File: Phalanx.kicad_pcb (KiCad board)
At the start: 2 copper layers, 19 x 95.2 mm, 7 parts, among them J1 Conn_01x05, J2 Conn_01x05, J3 Conn_01x05, SW1 SW_Push, SW2 SW_Push, SW3 SW_Push, SW4 SW_Push

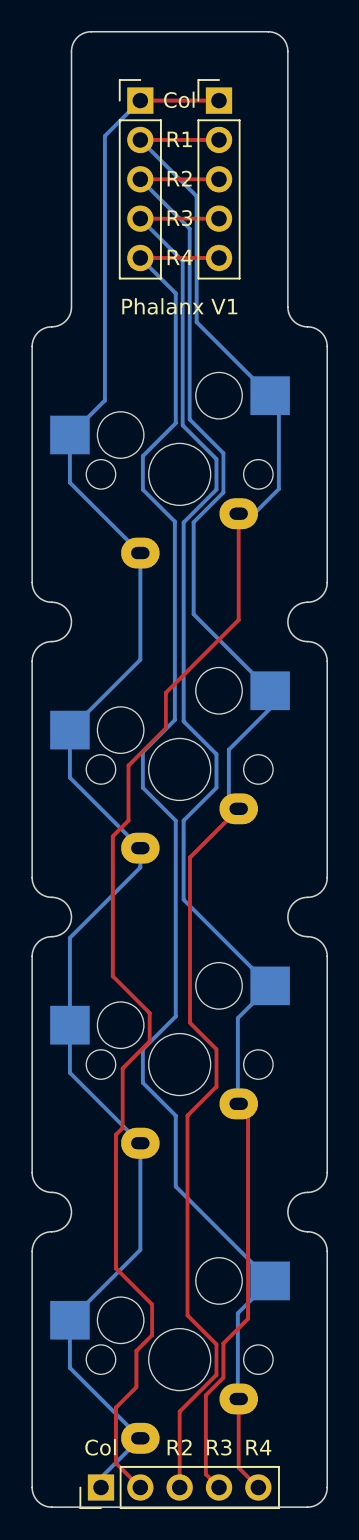
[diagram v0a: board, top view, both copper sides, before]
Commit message: fix dimensions
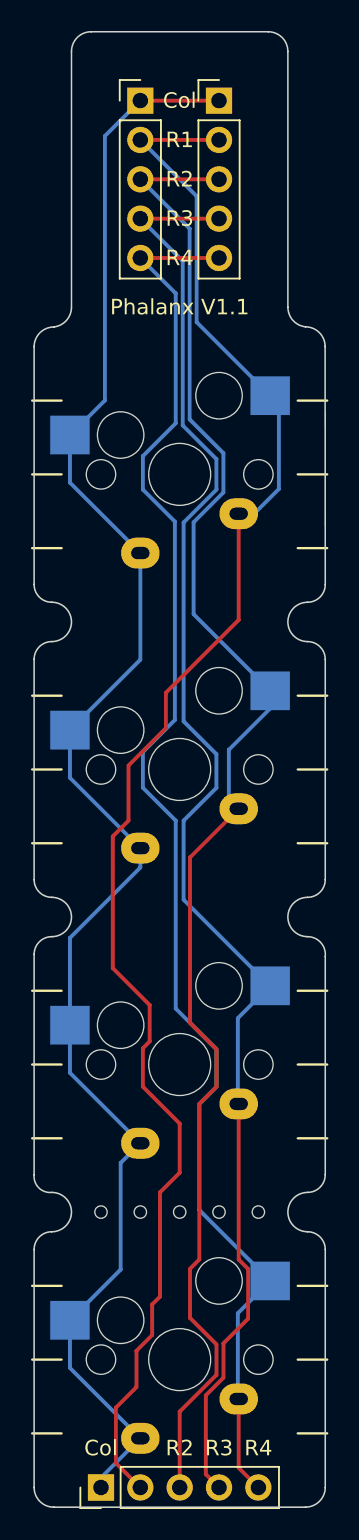
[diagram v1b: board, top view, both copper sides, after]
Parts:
- added REF**: break, Keyboard_JSA:break, F.Cu at (101.6, 126.4)
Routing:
- net Row4: track 94.6 -> 93.7 mm
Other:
- board size 19 x 95.2 mm -> 18.8 x 95.2 mm
- board text added: "JLCJLCJLCJLC"
- board text added: "Phalanx V1.1"
- board text removed: "Phalanx V1"
